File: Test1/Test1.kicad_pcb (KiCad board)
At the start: 2 copper layers, 165.1 x 83.8 mm, 75 parts, among them J1 Screw_Terminal_01x03, J2 Screw_Terminal_01x03, J3 Screw_Terminal_01x03, J4 Screw_Terminal_01x03, J5 Screw_Terminal_01x03, J6 Screw_Terminal_01x03, J7 Screw_Terminal_01x03, J8 Screw_Terminal_01x03, Q1 BC337, Q2 BC337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

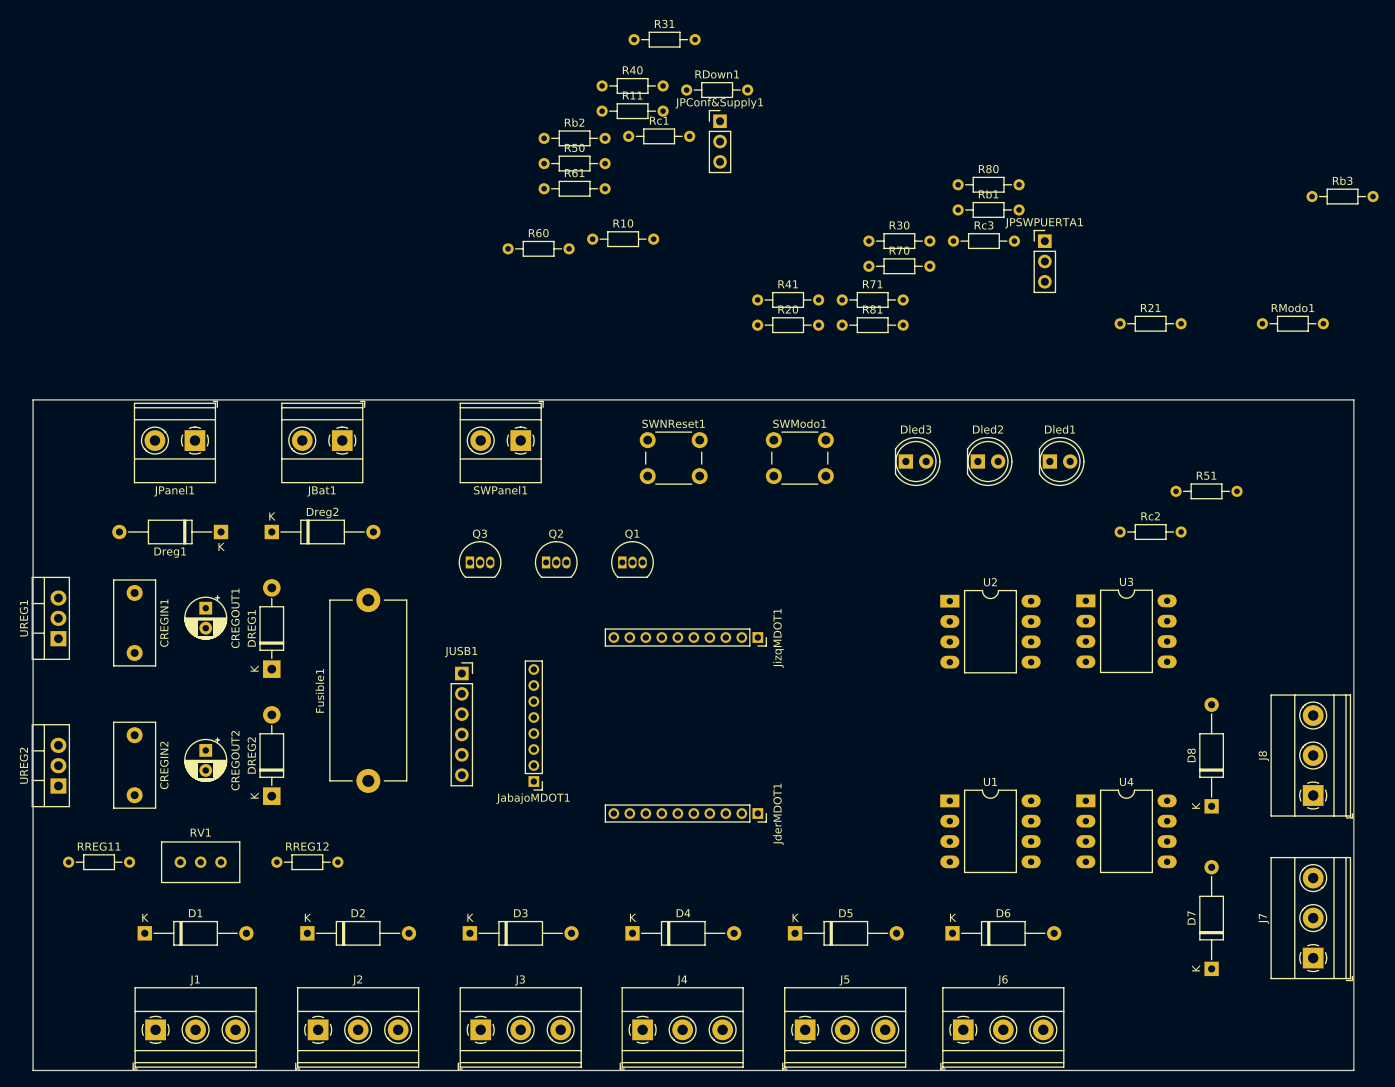
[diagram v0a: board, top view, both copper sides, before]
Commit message: Cambios antes de comenzar a rutear
Se modificaron algunas cosas en esquemático para comenzar a rutear.
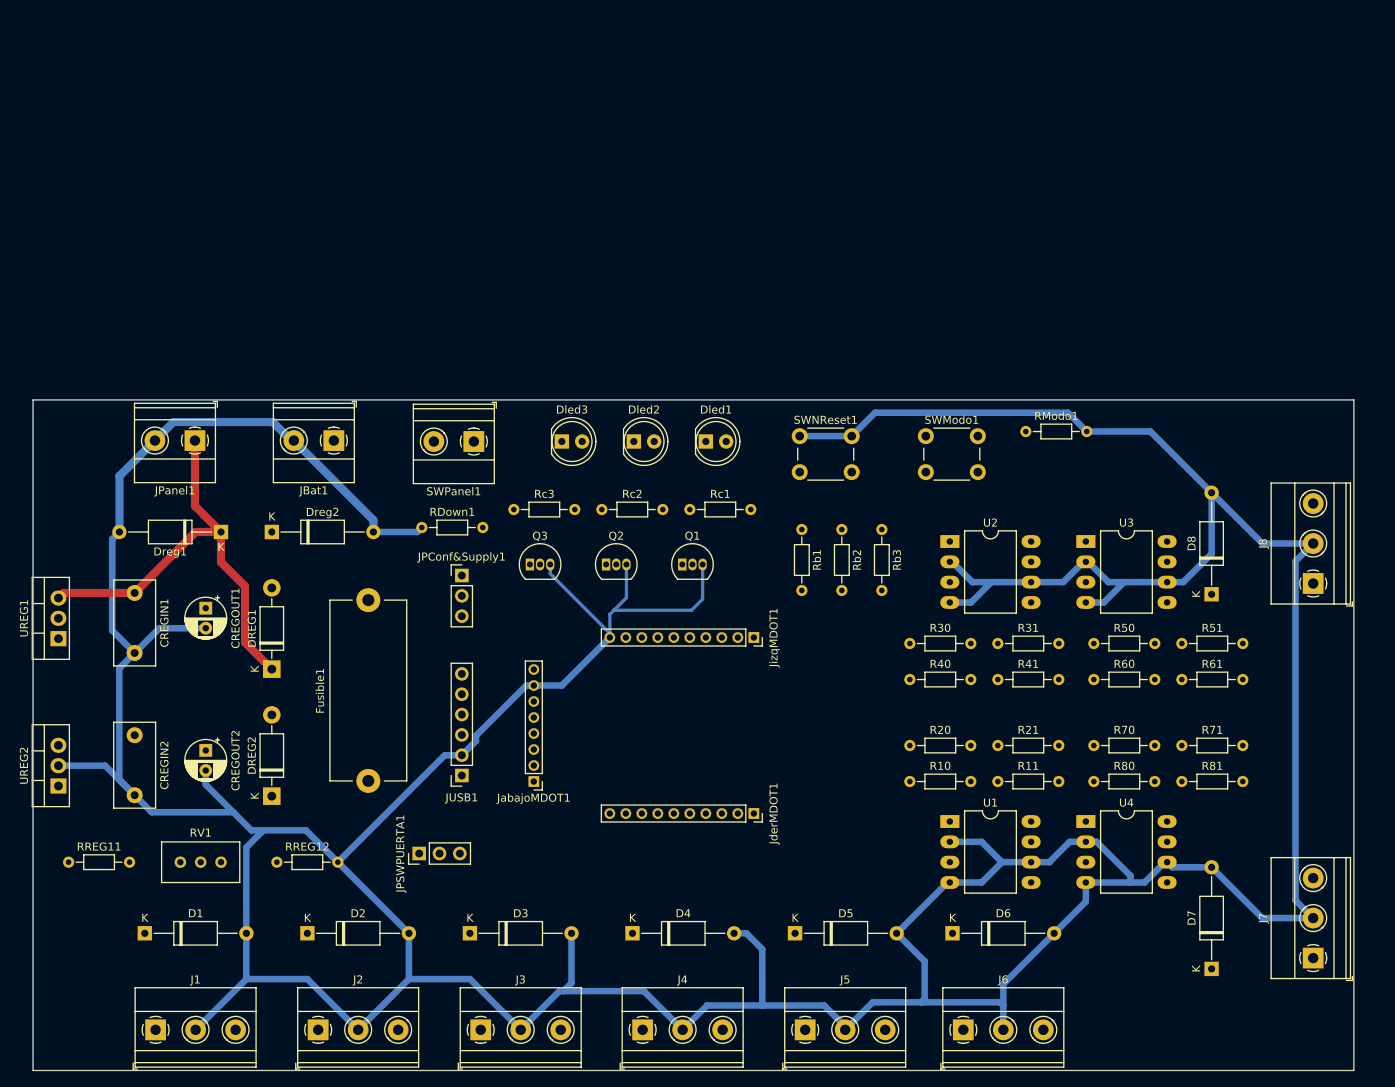
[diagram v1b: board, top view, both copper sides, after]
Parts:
- moved JPSWPUERTA1 109.4 mm to (137.2, 107.5), turned to 90 degrees
- moved R61 100.6 mm to (232.5, 85.8)
- moved R11 97.3 mm to (209.5, 98.5)
- moved R50 91.2 mm to (221.5, 81.2)
- moved R60 90.9 mm to (221.5, 85.8)
- moved R31 88.1 mm to (209.5, 81.2)
- moved R40 83.6 mm to (198.5, 85.8)
- moved R10 78.5 mm to (198.5, 98.5)
- moved R80 76.5 mm to (221.5, 98.5)
- moved R81 71.1 mm to (232.5, 98.5)
- moved R71 70.0 mm to (232.5, 94.0)
- moved Rb3 68.0 mm to (195.0, 67.0), turned to 270 degrees
- moved R70 66.2 mm to (221.5, 94.0)
- moved JPConf&Supply1 65.3 mm to (142.5, 72.8)
- moved Rc2 64.9 mm to (160.0, 64.5)
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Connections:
- R10 pad 2: +3V3 -> 3VMdot
- R11 pad 1: +3V3 -> 3VMdot
- R20 pad 2: +3V3 -> 3VMdot
- R21 pad 2: +3V3 -> 3VMdot
- R30 pad 2: +3V3 -> 3VMdot
- R31 pad 1: +3V3 -> 3VMdot
- R40 pad 2: +3V3 -> 3VMdot
- R41 pad 2: +3V3 -> 3VMdot
- R50 pad 2: +3V3 -> 3VMdot
- R51 pad 1: +3V3 -> 3VMdot
- R60 pad 2: +3V3 -> 3VMdot
- R61 pad 2: +3V3 -> 3VMdot
- R70 pad 2: +3V3 -> 3VMdot
- R71 pad 1: +3V3 -> 3VMdot
- R80 pad 2: +3V3 -> 3VMdot
- R81 pad 2: +3V3 -> 3VMdot
- U1 pad 8: +3V3 -> 3VMdot
- U2 pad 8: +3V3 -> 3VMdot
- U3 pad 8: +3V3 -> 3VMdot
- U4 pad 8: +3V3 -> 3VMdot
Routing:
- net GND: track 0.00 -> 695.4 mm
- net +12V: track 0.00 -> 56.3 mm

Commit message: Avance hasta el dia de la fecha con placa soldada y enviando datos.
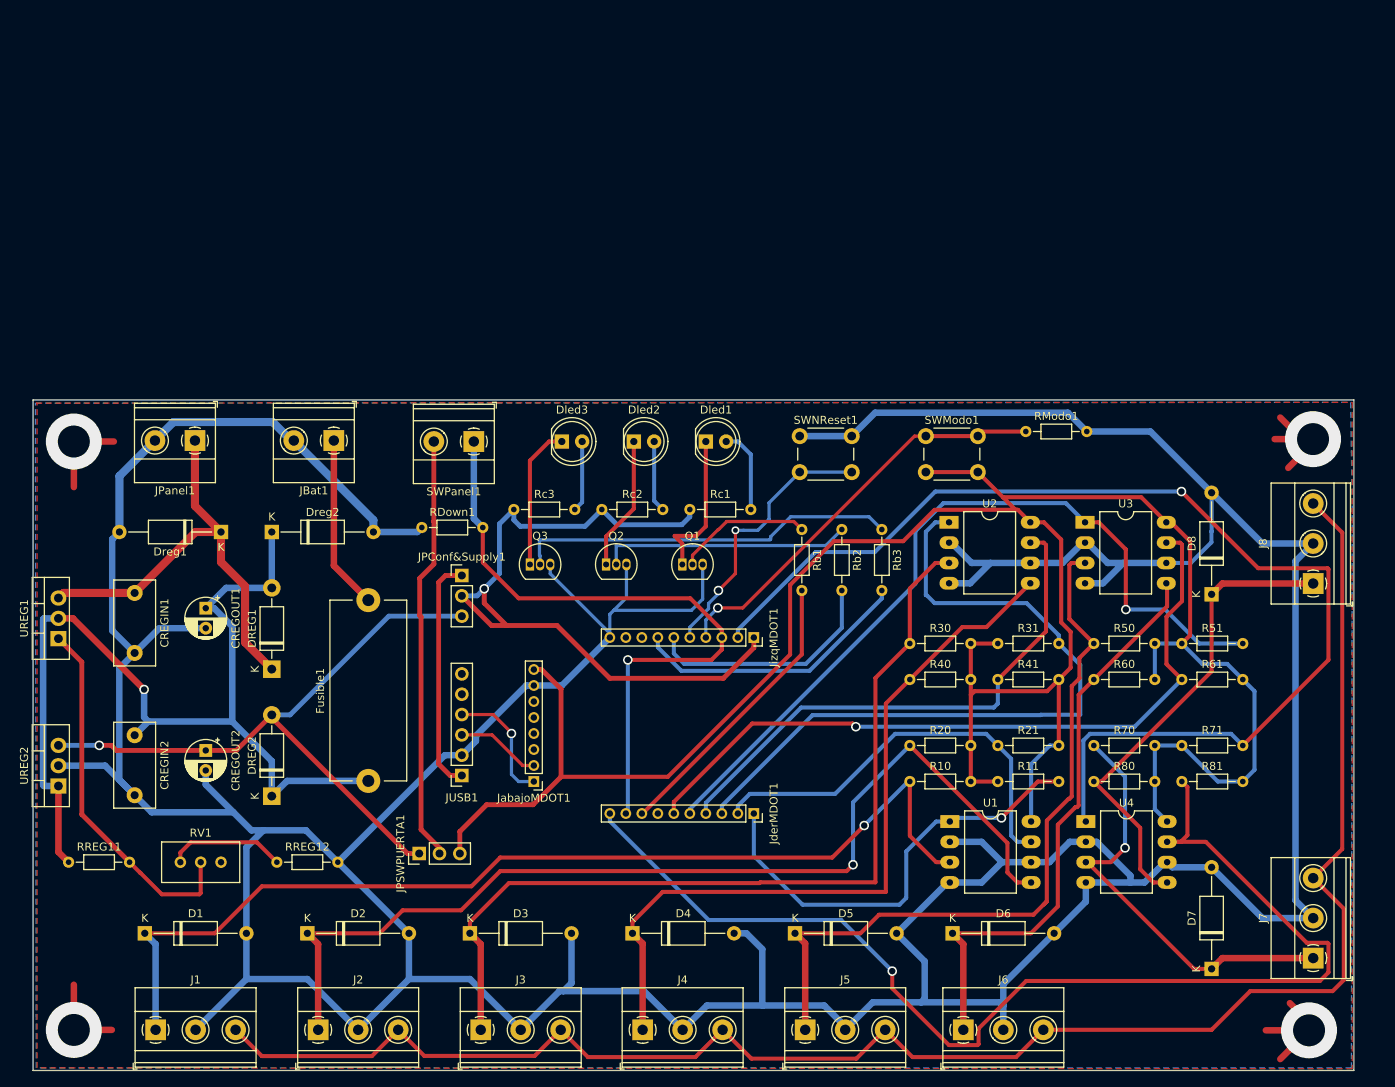
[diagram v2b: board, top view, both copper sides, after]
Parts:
- moved U2 2.40 mm to (203.4, 66.1)
- moved U3 2.40 mm to (220.4, 66.1)
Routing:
- net 3VMdot: track 0.00 -> 297.8 mm
- net Net-(J1-Pad3): track 0.00 -> 274.6 mm, vias 0 -> 4
- net VccMDOT: track 0.00 -> 174.1 mm, vias 0 -> 2
- net AI8: track 0.00 -> 147.5 mm, vias 0 -> 1
- net AI7: track 0.00 -> 143.6 mm, vias 0 -> 1
- net Net-(D1-Pad1): track 0.00 -> 129.4 mm, vias 0 -> 1
- net Net-(D2-Pad1): track 0.00 -> 126.6 mm, vias 0 -> 1
- net Vbat: track 0.00 -> 123.0 mm, vias 0 -> 1
- net Net-(D3-Pad1): track 0.00 -> 111.5 mm
- net AI5: track 0.00 -> 101.0 mm, vias 0 -> 1
- net Net-(D4-Pad1): track 0.00 -> 95.1 mm
- net Net-(D5-Pad1): track 0.00 -> 94.2 mm
- net AI6: track 0.00 -> 92.1 mm, vias 0 -> 1
- net AI3: track 0.00 -> 91.5 mm
- net DIPuerta: track 0.00 -> 83.0 mm, vias 0 -> 1
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- added copper zone on B.Cu, net GND
- added copper zone on F.Cu, net Net-(J1-Pad3)
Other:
- net class PAT Ins added: clearance 0.508, trace_width 1.016, via_dia 1.2, via_drill 0.8
- rule via_min_drill: 0.8 -> 0.6
- rule via_min_size: 1.2 -> 1

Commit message: Hasta acá se arreglaron los problemas de K
Funciona todo, envía ok, tanto caudal como frecuencia y se despierta si hay un cable cortado. Calcula correctamente y se puede configurar por usb. Falta probar panel conectado y luego la batería.
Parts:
- Dreg1, Dreg2: footprint Diode_THT:D_A-405_P12.70mm_Horizontal -> Diode_THT:D_DO-15_P15.24mm_Horizontal
- moved JUSB1 2.50 mm to (145.0, 97.7)
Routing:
- net GND: track 693.6 -> 683.6 mm
- net Net-(JUSB1-Pad4): track 15.5 -> 13.0 mm
- net Net-(JUSB1-Pad3): track 10.6 -> 8.11 mm
- net 5VUSB: track 29.5 -> 32.0 mm
